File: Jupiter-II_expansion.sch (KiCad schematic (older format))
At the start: 41 parts, among them J1 Conn_02x25_Odd_Even, J2 Conn_02x25_Odd_Even, J3 Conn_01x10, J4 Conn_01x03, U1 GAL22V10, U2 27C128, U3 628128, U4 AY-3-8910, U5 16C450, X1 CXO_DIP14 3.6864 MHz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

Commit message: First working version
Hardware validation
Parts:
- added R53, R54: 10k, Resistor_SMD:R_0805_2012Metric_Pad1.15x1.40mm_HandSolder, symbol Device:R
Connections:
- net +5V: now also R53.2, R54.2
- net XPAGE0: now also R54.1
- net XPAGE1: now also R53.1
- net ~CPAGE renamed CPAGE
- net ~SPAGE renamed SPAGE
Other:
- note added: "/* Memory Expansion: [4000-FFFF] */\nXROM = MREQ & XPAGE1 & XPAGE0 & A15 & A14 ; /* C000-FFFF */\nXRAM = MREQ & (A14 # A15) & !(XPAGE1 & XPAGE0 & A15 & A14) ; /* 4000 to FFFF */\nXA15 = XPAGE0 # !A15 ;\nXA16 = XPAGE1 # !A15 ;\n\n/* Programmable Sound Generator: odd I/O [F1-FF] */\nPSG = IORQ & A7 & A6 & A5 & A4 & A0; /* I/O: 1111 xxx1 */\nPSGBDIR = PSG & WR;\nPSGBC1 = PSG & (WR $ A1);\n\n/* Seria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"
- note added: "128Kx8 SRAM alternatives:\n TC551001PL\n KM681000ALP\n SRM20100LC\n"
- note added: "FORTH definitions\n(Note: When using PSG keep Register R7 bits 6 and 7 setted \notherwise Colours and Memory paging will be affected )\n\n( Select PSG Register to Read/Write )\n: PSG> ( register -- ) 253 OUT ;\n\n( Read from PSG Register )\n: PSG@ ( register -- value ) PSG> 255 IN ;\n\n( Write to PSG Register )\n: PSG! ( value register -- ) PSG> 255 OUT ;\n\n( Set/Get INK, PAPER colour )\n: PORTA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"
- note added: "XPAGE1, XPAGE0, A15, A14 -> XA16, XA15\n xx00 -> xx XRAM, XROM disabled\n --01 -> 11 Unpaged 16K XRAM (A14=1)\n 0010 -> 00 16K XRAM(a) (XA14=0)\n 0011 -> 00 16K XRAM(b) (XA14=1)\n 0110 -> 01 16K XRAM(c) (XA14=0)\n 0111 -> 01 16K XRAM(d) (XA14=1)\n 1010 -> 10 16K XRAM(e) (XA14=0)\n 1011 -> 10 16K XRAM(f) (XA14=1)\n 1110 -> 11 16K XRAM(g) (XA14=0)\n 1111 -> xx 16K XROM"
- note removed: "/* Memory Expansion: MEM [4000-FFFF] */\nXROM = MREQ & !XPAGE1 & !XPAGE0 & A15 & A14 ; /* C000-FFFF */\nXRAM = MREQ & (A14 # A15) & !XROM ; /* 4000 to FFFF */\nXA15 = XPAGE0 & A15 ;\nXA16 = XPAGE1 & A15 ;\n\n/* Programmable Sound Generator: odd I/O [F1-FF] */\nPSG = IORQ & A7 & A6 & A5 & A4 & A0; /* I/O: 1111 xxx1 */\nPSGBDIR = PSG & WR;\nPSGBC1 = PSG & (WR $ A1);\n\n/* Serial Interface: odd I/O 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"
- note removed: "Alternatives to 628128 (128Kx8 SRAM ):\n TC551001PL\n KM681000ALP\n SRM20100LC\n"
- note removed: "Note: \nWhen using PSG keep Register R7 bits 6 and 7 setted \notherwise Colours will be disabled and\nMemory paging will reset.\n\n( Select PSG Register to Read/Write )\n: PSGREG ( register -- ) 253 OUT ;\n\n( Read from PSG Register )\n: PSG@ ( register -- value ) PSGREG 255 IN ;\n\n( Write to PSG Register )\n: PSG! ( value register -- ) PSGREG 255 OUT ;\n\n(Initialize PSG Ports as outputs)\n: PS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"
- moved on the sheet: U2, U3

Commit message: Text corrections
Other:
- note added: "Colour Palette\n\nIRGB Color\n0000 Black\n0001 Blue\n0010 Green\n0011 Cyan\n0100 Red\n0101 Magenta\n0110 Dark Yellow\n0111 Light Gray\n1000 Dark Gray\n1001 Light Blue\n1010 Light Green\n1011 Light Cyan\n1100 Light Red\n1101 Light Magenta\n1110 Yellow\n1111 White"
- note added: "GAL22V10 Logic:\n\nXROM = MREQ & XPAGE1 & XPAGE0 & A15 & A14 ;\nXRAM = MREQ & (A14 # A15) & !(XPAGE1 & XPAGE0 & A15 & A14) ; \nXA15 = XPAGE0 # !A15 ;\nXA16 = XPAGE1 # !A15 ;\n\nPSG = IORQ & A7 & A6 & A5 & A4 & A0 ;\nPSGBDIR = PSG & WR ;\nPSGBC1 = PSG & (WR $ A1) ;\n\nUART = IORQ & A7 & A6 & A5 & !A4 & A0 ;\nUARTRST = RESET ;\n"
- note added: "Possible AY-3-8910 replacements: (not tested!)\n Yamaha YM2149F, YM3439-D, Toshiba T7766A,\n Winbond WF19054, JFC 95101, File KC89C72\n Microchip AY-3-8930 (or AY8930)\n\nI/O Addressing compatible with EME Sound Card\n 253 (FD) : Select Register, \n 255 (FF) : Read/Write Register Value\n\nBDIR BC1\n 0 0 Read 253 (FD = 1111 1101): Inactive\n 0 1 Read 255 (FF = 1111 1111): Read from PSG Register\n 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"
- note added: "Reset State:\nXPAGE = 3"
- note added: "_____UART_____________________________________\n225 (E1) : Receiver Buffer Register: Read\n Transmitter Holding Register: Write\n Divisor Latch LSB (DLAB=1)\n227 (E3) : Interrupt Enable Register\n Divisor Latch MSB (DLAB=1)\n229 (E5) : Interrupt Identifier Register: Read\n231 (E7) : Line Control Register\n233 (E9) : Modem Control Register\n235 (EB) : Line Status Register\n237 (ED) : Modem Status 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"
- note removed: "/* Memory Expansion: [4000-FFFF] */\nXROM = MREQ & XPAGE1 & XPAGE0 & A15 & A14 ; /* C000-FFFF */\nXRAM = MREQ & (A14 # A15) & !(XPAGE1 & XPAGE0 & A15 & A14) ; /* 4000 to FFFF */\nXA15 = XPAGE0 # !A15 ;\nXA16 = XPAGE1 # !A15 ;\n\n/* Programmable Sound Generator: odd I/O [F1-FF] */\nPSG = IORQ & A7 & A6 & A5 & A4 & A0; /* I/O: 1111 xxx1 */\nPSGBDIR = PSG & WR;\nPSGBC1 = PSG & (WR $ A1);\n\n/* Seria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"
- note removed: "FORTH definitions\n(Note: When using PSG keep Register R7 bits 6 and 7 setted \notherwise Colours and Memory paging will be affected )\n\n( Select PSG Register to Read/Write )\n: PSG> ( register -- ) 253 OUT ;\n\n( Read from PSG Register )\n: PSG@ ( register -- value ) PSG> 255 IN ;\n\n( Write to PSG Register )\n: PSG! ( value register -- ) PSG> 255 OUT ;\n\n( Set/Get INK, PAPER colour )\n: PORTA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"
- note removed: "XPAGE1, XPAGE0, A15, A14 -> XA16, XA15\n xx00 -> xx XRAM, XROM disabled\n --01 -> 11 Unpaged 16K XRAM (A14=1)\n 0010 -> 00 16K XRAM(a) (XA14=0)\n 0011 -> 00 16K XRAM(b) (XA14=1)\n 0110 -> 01 16K XRAM(c) (XA14=0)\n 0111 -> 01 16K XRAM(d) (XA14=1)\n 1010 -> 10 16K XRAM(e) (XA14=0)\n 1011 -> 10 16K XRAM(f) (XA14=1)\n 1110 -> 11 16K XRAM(g) (XA14=0)\n 1111 -> xx 16K XROM"
- note removed: "_____PSG_______________________________________\nAY-3-8910 Programmable Sound Generator\nI/O Addressing compatible with EME Sound Card\nFDh (253): select Register, \nFFh (255): read/write Register Value\n\nBDIR BC1\n 0 0 Read 253 (FDh = 1111 1101): Inactive\n 0 1 Read 255 (FFh = 1111 1111): Read from PSG Register\n 1 0 Write 255 (FFh = 1111 1111): Write to PSG Register\n 1 1 Write 253 (FDh = 1111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"
- note removed: "_____UART_____________________________________\nUART = IORQ & A0 & ADDRS:[E1..EF] ;\n\nE1h (225): RBR - Receiver Buffer Register: Read\n THR - Transmitter Holding Register: Write\n DLL - Divisor Latch LSB (DLAB=1)\nE3h (227): IER - Interrupt Enable Register\n DLM - Divisor Latch MSB (DLAB=1)\nE5h (229): IIR - Interrupt Identifier Register: Read\nE7h (231): LCR - Line Control Register\nE9h (233): 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"
- moved on the sheet: U2, U3

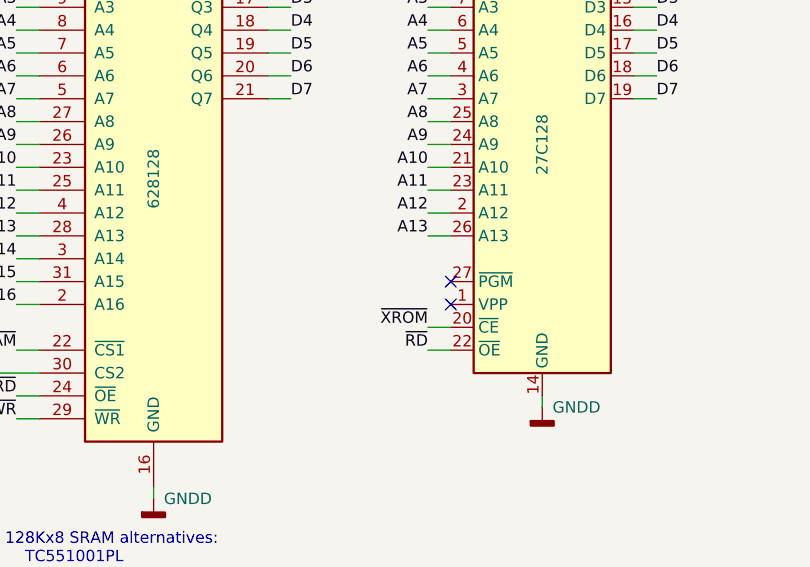
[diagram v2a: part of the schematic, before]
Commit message: Corrected missing connections on XROM
Corrected missing connections on XROM pins 1 and 27
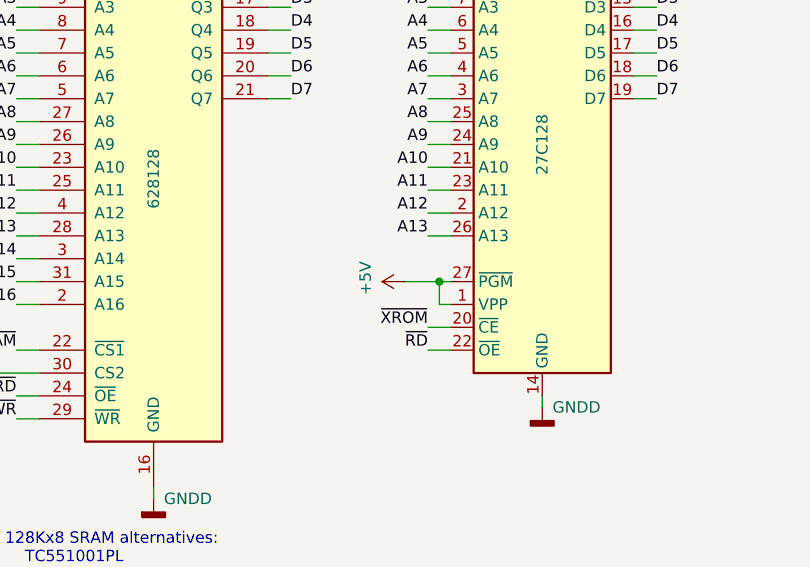
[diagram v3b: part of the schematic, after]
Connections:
- net +5V: now also U2.1 (VPP), U2.27 (~PGM)
- no-connect marks 17 -> 15
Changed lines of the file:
@@
 Text Label 13800 2850 2    50   ~ 0
 A13
-NoConn ~ 13900 3050
-NoConn ~ 13900 3150
 Text Label 13800 3350 2    50   ~ 0
 ~RD
@@
 	6700 3200 6500 3200
 Connection ~ 6500 3200
+Text Notes 4250 7000 0    50   ~ 0
+Colour Palette\n\nIRGB  Color\n0000 Black\n0001 Blue\n0010 Green\n0011 Cyan\n0100 Red\n0101 Magenta\n0110 Dark Yellow\n0111 Light Gray\n1000 Dark Gray\n1001 Light Blue\n1010 Light Green\n1011 Light Cyan\n1100 Light Red\n1101 Light Magenta\n1110 Yellow\n1111 White
+Text Notes 6650 3550 0    50   ~ 0
+Reset State:\nXPAGE = 3
+$Comp
+L power:+5V #PWR?
+U 1 1 5F38E533
+P 13700 3050
+AR Path="/5E875CD1/5F38E533" Ref="#PWR?"  Part="1"
+AR Path="/5F38E533" Ref="#PWR?"  Part="1"
+F 0 "#PWR?" H 13700 2900 50  0001 C CNN
+F 1 "+5V" H 13715 3223 50  0000 C CNN
+F 2 "" H 13700 3050 50  0001 C CNN
+F 3 "" H 13700 3050 50  0001 C CNN
+	1    13700 3050
+	0    -1   -1   0
+$EndComp
+Wire Wire Line
+	13900 3150 13850 3150
+Wire Wire Line
+	13850 3150 13850 3050
+Wire Wire Line
+	13850 3050 13900 3050
+Wire Wire Line
+	13700 3050 13850 3050
 Wire Bus Line
 	7000 5200 7000 6400
 Wire Bus Line
 	7200 5050 7200 6000
-Text Notes 4250 7000 0    50   ~ 0
-Colour Palette\n\nIRGB  Color\n0000 Black\n0001 Blue\n0010 Green\n0011 Cyan\n0100 Red\n0101 Magenta\n0110 Dark Yellow\n0111 Light Gray\n1000 Dark Gray\n1001 Light Blue\n1010 Light Green\n1011 Light Cyan\n1100 Light Red\n1101 Light Magenta\n1110 Yellow\n1111 White
-Text Notes 6650 3550 0    50   ~ 0
-Reset State:\nXPAGE = 3
+Connection ~ 13850 3050
 $EndSCHEMATC

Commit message: Added missing library
Added missing library and PDF schematic
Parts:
- removed U1: GAL22V10, Package_DIP:DIP-24_W7.62mm_Socket, symbol Jupiter-Ace+-rescue:GAL22V10-rfl_pld
- added U1: GAL22V10, symbol rfl_pld:GAL22V10
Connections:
- net +5V: now also U1.24 (VCC)
- net A0: now also U1.11 (I)
- net A1: now also U1.10 (I)
- net A14: now also U1.5 (I)
- net A15: now also U1.4 (I)
- net A4: now also U1.9 (I)
- net A5: now also U1.8 (I)
- net A6: now also U1.7 (I)
- net A7: now also U1.6 (I)
- net GNDD: now also U1.12 (GND)
- net PSGBC1: now also U1.16 (I/O)
- net PSGBDIR: now also U1.17 (I/O)
- net UARTRST: now also U1.23 (I/O)
- net XA15: now also U1.21 (I/O)
- net XA16: now also U1.20 (I/O)
- net XPAGE0: now also U1.15 (I/O)
- net XPAGE1: now also U1.14 (I/O)
- net ~IORQ: now also U1.2 (I)
- net ~MREQ: now also U1.1 (I/CK)
- net ~RESET: now also U1.13 (I)
- net ~UART: now also U1.22 (I/O)
- net ~WR: now also U1.3 (I)
- net ~XRAM: now also U1.19 (I/O)
- net ~XROM: now also U1.18 (I/O)
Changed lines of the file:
@@
-$EndComp
-$Comp
-L Jupiter-Ace+-rescue:GAL22V10-rfl_pld U?
-U 1 1 5E9E8CDF
-P 5800 2100
-AR Path="/5C72F810/5E9E8CDF" Ref="U?"  Part="1"
-AR Path="/5C8BA3E4/5E9E8CDF" Ref="U?"  Part="1"
-AR Path="/5E9E8CDF" Ref="U1"  Part="1"
-AR Path="/5E8292A6/5E9E8CDF" Ref="U?"  Part="1"
-F 0 "U1" H 5950 2850 50  0000 C CNN
-F 1 "GAL22V10" V 5800 2100 50  0000 C CNN
-F 2 "Package_DIP:DIP-24_W7.62mm_Socket" H 5850 2050 60  0001 C CNN
-F 3 "" H 5850 2050 60  0001 C CNN
-	1    5800 2100
-	1    0    0    -1
 $EndComp
 $Comp
@@
 Wire Wire Line
 	13700 3050 13850 3050
+Connection ~ 13850 3050
 Wire Bus Line
 	7000 5200 7000 6400
 Wire Bus Line
 	7200 5050 7200 6000
-Connection ~ 13850 3050
+$Comp
+L rfl_pld:GAL22V10 U1
+U 1 1 5F8C823C
+P 5800 2100
+F 0 "U1" H 5950 2850 50  0000 C CNN
+F 1 "GAL22V10" V 5800 2100 50  0000 C CNN
+F 2 "" H 5850 2050 60  0000 C CNN
+F 3 "" H 5850 2050 60  0000 C CNN
+	1    5800 2100
+	1    0    0    -1
+$EndComp
 $EndSCHEMATC
